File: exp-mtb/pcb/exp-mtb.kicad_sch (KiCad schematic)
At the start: 71 parts, among them J1 Conn_02x08, J2 Conn_02x05, J3 Conn_01x02, J4 Conn_01x02, J5 AVR-ISP-6, Q1 BT148, SW1 SW_Push, U1 ADUM1250, U2 6N137, U3 6N137, U4 ATmega328P-AU, U5 L78L05_SOT89, U6 SN75176AD, U7 PC817, Y1 14.745 MHz

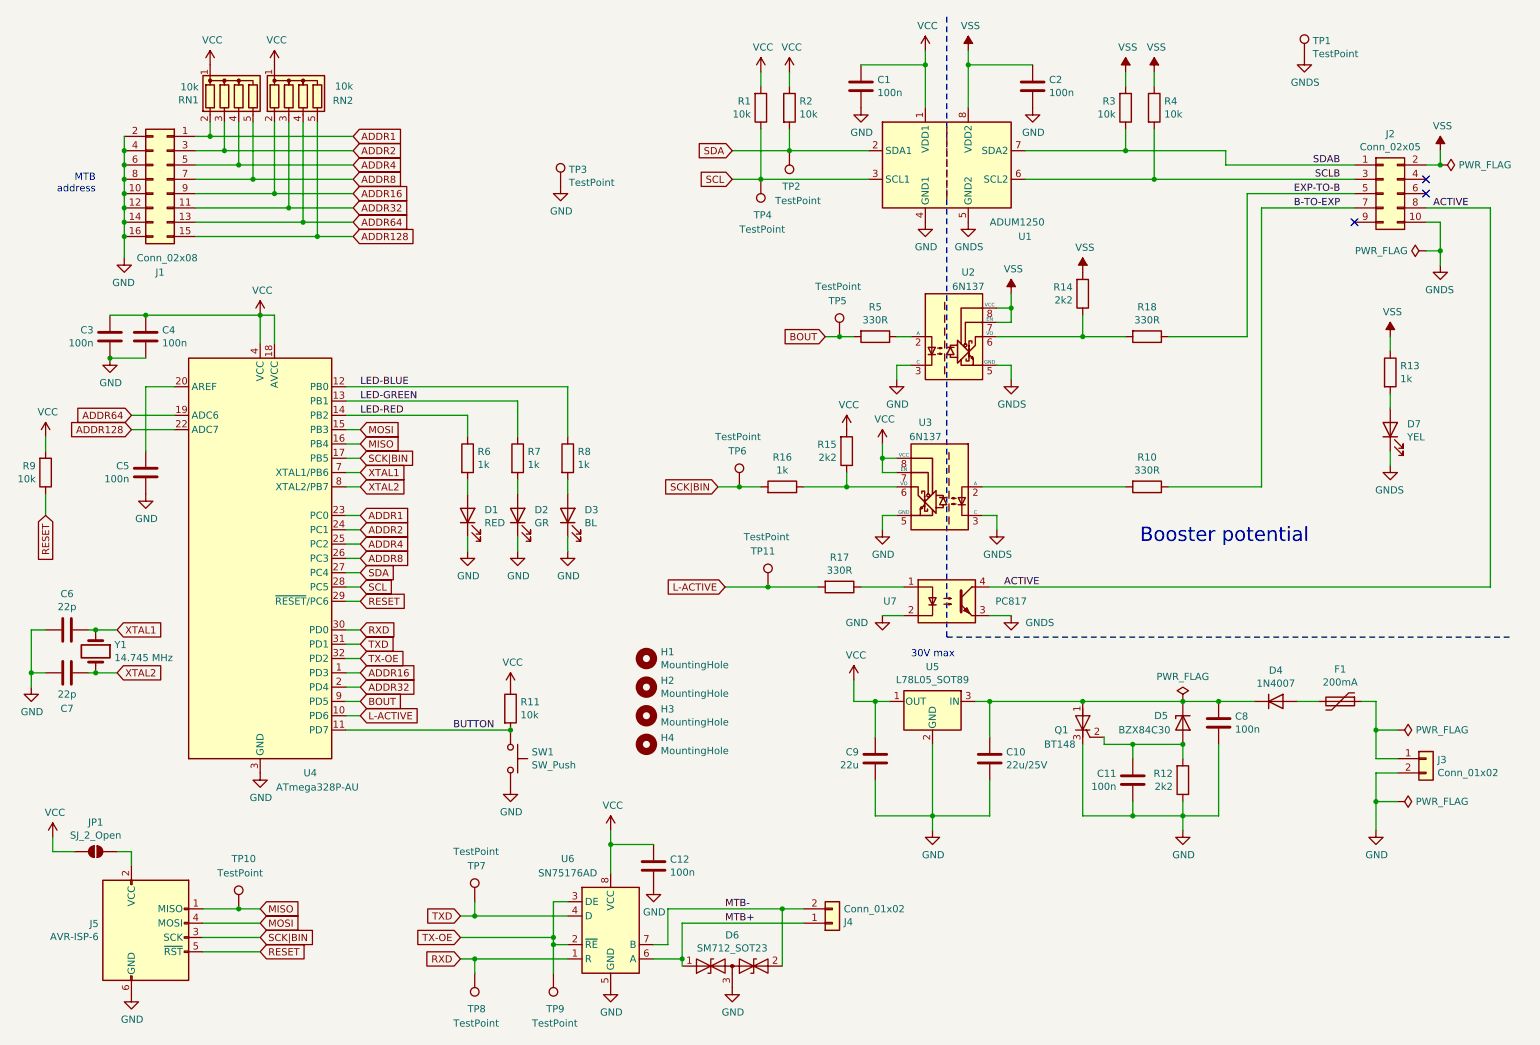
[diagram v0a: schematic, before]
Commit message: exp-mtb: move pcb to 'pcb' directory.
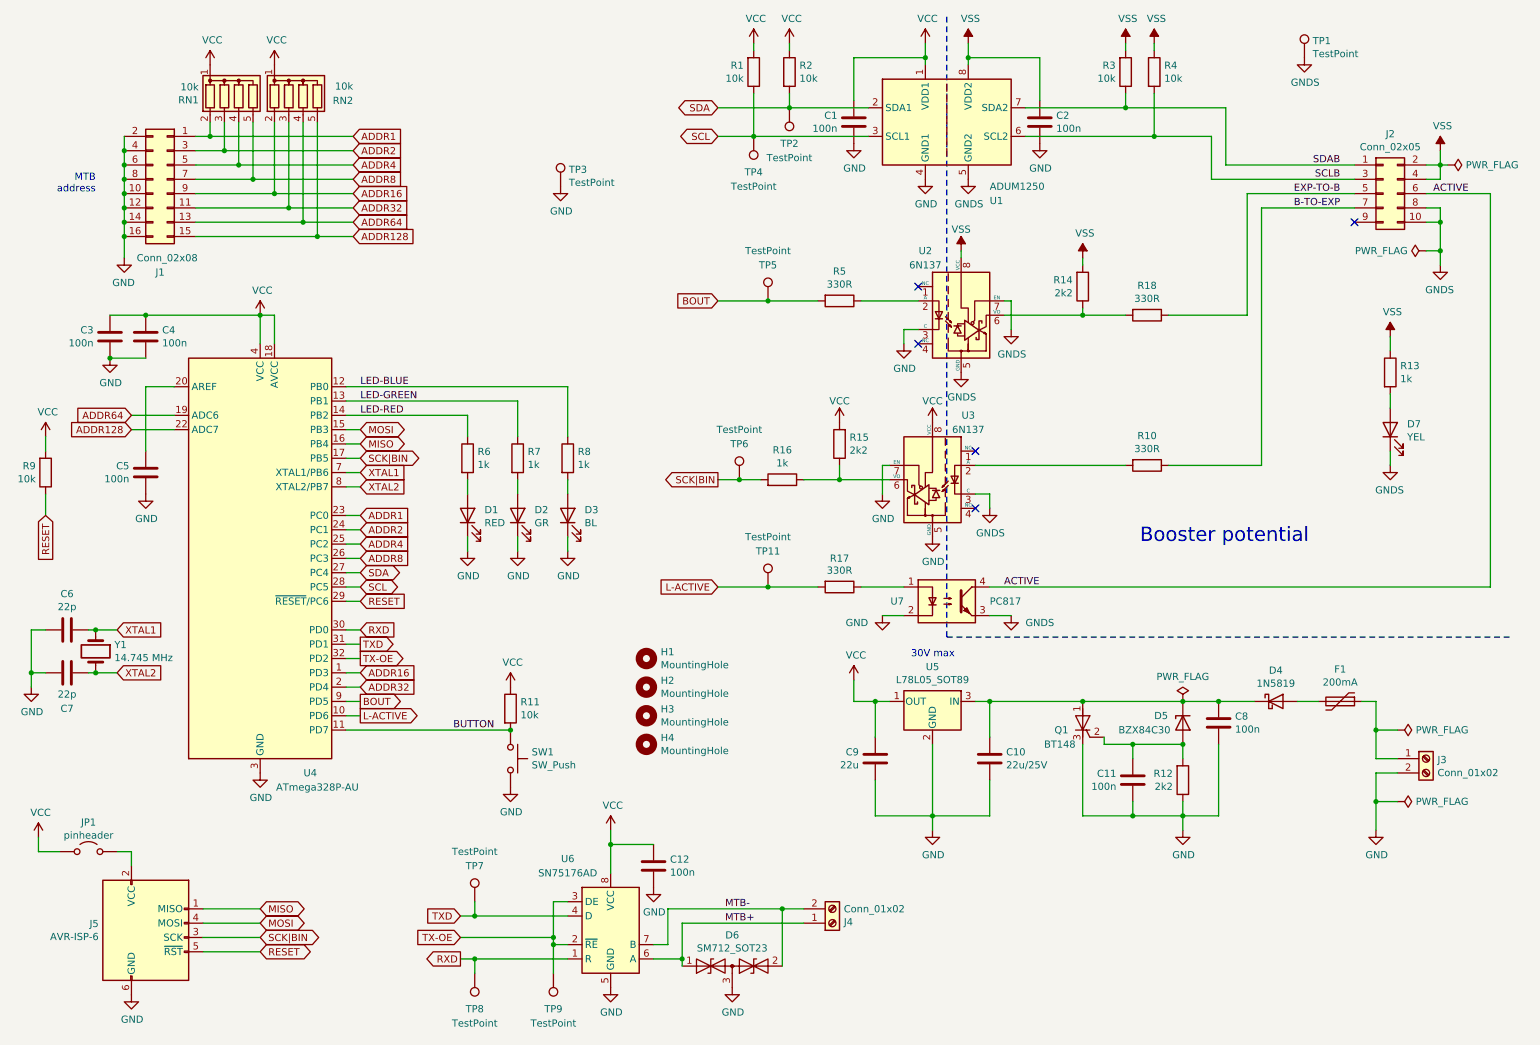
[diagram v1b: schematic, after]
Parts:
- removed TP10: TestPoint, TestPoint:TestPoint_Pad_D1.0mm, symbol Connector:TestPoint
- D4: value 1N4007 -> 1N5819; footprint Diode_SMD:D_SOD-323_HandSoldering -> Diode_SMD:D_SOD-123; symbol Diode:1N4007 -> Diode:1N5819
- D5: footprint Diode_SMD:D_SOT-23_ANK -> Package_TO_SOT_SMD:SOT-23; symbol exp-mtb-rescue:BZX84Cxx-Diode -> Diode:BZX84Cxx
- D6: footprint Package_TO_SOT_SMD:SOT-23_Handsoldering -> Package_TO_SOT_SMD:SOT-23
- J3, J4: symbol Connector_Generic:Conn_01x02 -> Connector:Screw_Terminal_01x02
- JP1: value SJ_2_Open -> pinheader; symbol Jumper:SolderJumper_2_Open -> Jumper:Jumper_2_Open
- Q1: footprint Package_TO_SOT_SMD:SOT-223 -> Package_TO_SOT_THT:TO-92_Inline
- RN1, RN2: footprint Resistor_SMD:R_Array_Concave_4x0603 -> Resistor_THT:R_Array_SIP5
- U2, U3: footprint Package_DIP:SMDIP-8_W7.62mm -> Package_DIP:DIP-8_W7.62mm; symbol exp-mtb-rescue:6N137-Isolator -> Isolator:6N137
- U4: symbol exp-mtb-rescue:ATmega328P-AU-MCU_Microchip_ATmega -> MCU_Microchip_ATmega:ATmega328P-A
- U5: footprint Package_TO_SOT_SMD:SOT-89-3_Handsoldering -> Package_TO_SOT_SMD:SOT-89-3
- U6: footprint Package_DIP:DIP-8_W7.62mm_LongPads -> Package_SO:SOIC-8_3.9x4.9mm_P1.27mm
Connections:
- net ACTIVE: now also J2.6 (Pin_6); no longer J2.8 (Pin_8)
- net GND: now also U3.7 (EN)
- net GNDS: now also J2.8 (Pin_8), U2.7 (EN)
- net VCC: no longer U3.7 (EN)
- net VSS: now also J2.4 (Pin_4); no longer U2.7 (EN)
- net at C10.1, C8.1, D4.1 (K)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: now also D5.3 (K); no longer D5.1 (K)
- net at C11.2, Q1.2 (G), R12.2: now also D5.1 (A); no longer D5.2 (A)
- no-connect marks 3 -> 5
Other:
- moved on the sheet: C1, C2, R1, R10, R14, R15, R16, R18, R2, R3, R4, R5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

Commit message: exp-mtb: remove address jumpers.
Address will be set in EEPROM.
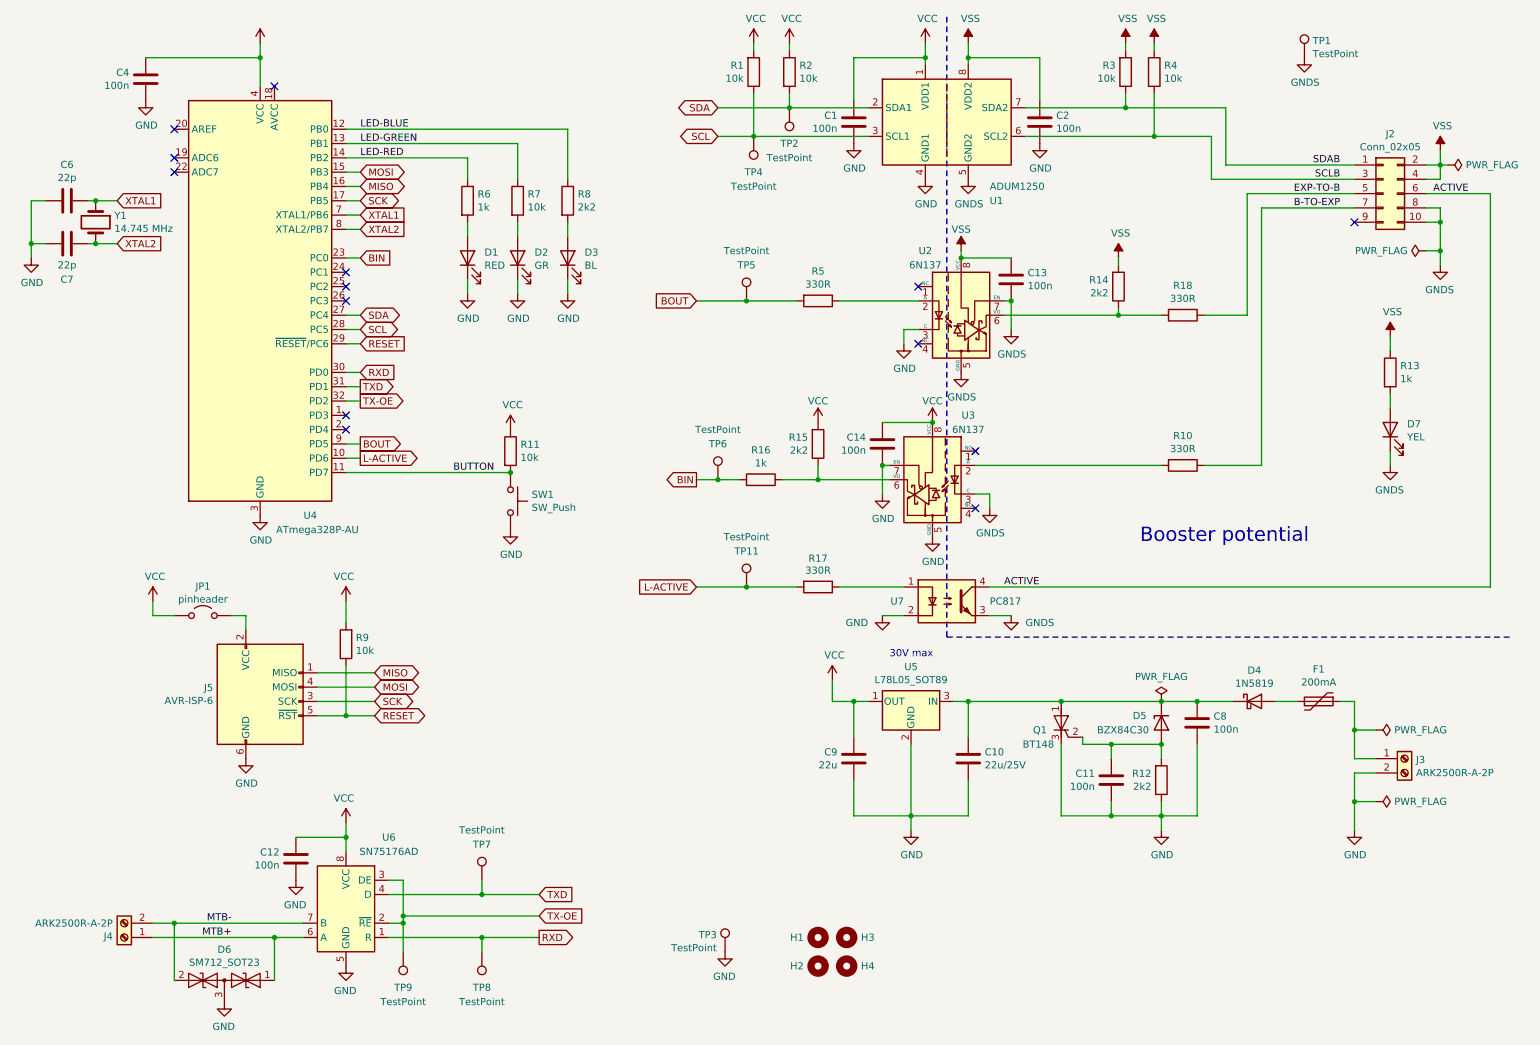
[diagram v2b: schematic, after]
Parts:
- removed C3, C5: 100n, Capacitor_SMD:C_0805_2012Metric_Pad1.18x1.45mm_HandSolder, symbol Device:C
- removed J1: Conn_02x08, Connector_PinHeader_2.54mm:PinHeader_2x08_P2.54mm_Vertical, symbol Connector_Generic:Conn_02x08_Odd_Even
- removed RN1, RN2: 10k, Resistor_THT:R_Array_SIP5, symbol Device:R_Network04
- added C13, C14: 100n, Capacitor_SMD:C_0805_2012Metric_Pad1.18x1.45mm_HandSolder, symbol Device:C
- H1, H2, H3, H4: value MountingHole -> ~
- J3, J4: value Conn_01x02 -> ARK2500R-A-2P; footprint TerminalBlock:TerminalBlock_bornier-2_P5.08mm -> Connector_Phoenix_MSTB:PhoenixContact_MSTBA_2,5_2-G_1x02_P5.00mm_Horizontal
- JP1: footprint Jumper:SolderJumper-2_P1.3mm_Open_RoundedPad1.0x1.5mm -> Connector_PinHeader_2.54mm:PinHeader_1x02_P2.54mm_Vertical
- R7: value 1k -> 10k
- R8: value 1k -> 2k2
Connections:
- net GND: now also C14.2
- net GNDS: now also C13.2
- net VCC: now also C14.1; no longer U4.18 (AVCC)
- net VSS: now also C13.1
- net ADDR1 renamed BIN
- net BIN: now also R16.2, TP6.1
- net ADDR128: no longer names the net of U4.22 (ADC7)
- net ADDR16: no longer names the net of U4.1 (PD3)
- net ADDR2: no longer names the net of U4.24 (PC1)
- net ADDR32: no longer names the net of U4.2 (PD4)
- net ADDR4: no longer names the net of U4.25 (PC2)
- net ADDR64: no longer names the net of U4.19 (ADC6)
- net ADDR8: no longer names the net of U4.26 (PC3)
- net SCK|BIN renamed SCK
- net SCK: no longer R16.2, TP6.1
- no-connect marks 5 -> 14
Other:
- note removed: "MTB address"
- moved on the sheet: C10, C11, C12, C4, C6, C7, C8, C9, D1, D2, D3, D4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

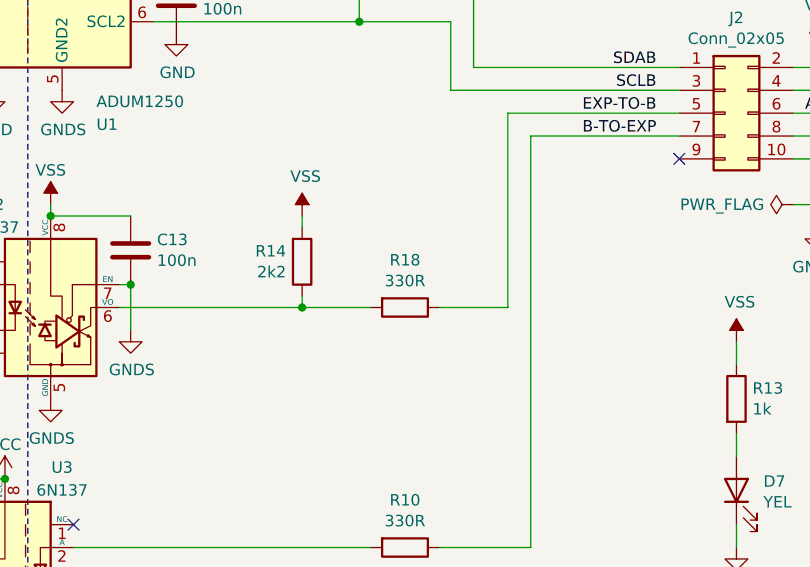
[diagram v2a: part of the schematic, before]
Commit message: Use polyfuse instead of resistor for main-exp protection.
Make voltage measurement possible.
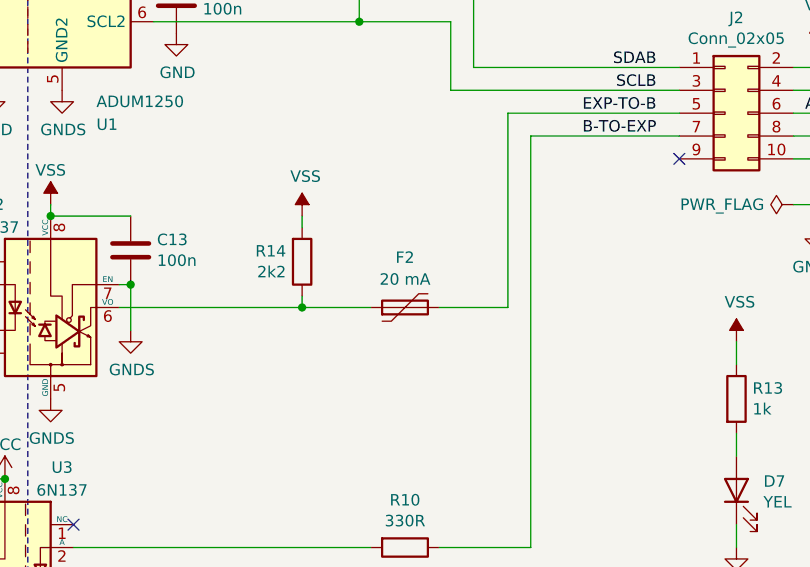
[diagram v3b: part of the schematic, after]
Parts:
- removed R18: 330R, Resistor_SMD:R_0805_2012Metric_Pad1.20x1.40mm_HandSolder, symbol Device:R
- added F2: 20 mA, symbol Device:Polyfuse
- U2, U3: footprint Package_DIP:DIP-8_W7.62mm -> Package_DIP:DIP-8_W8.89mm_SMDSocket_LongPads
- U7: footprint Package_DIP:DIP-4_W7.62mm -> Package_DIP:DIP-4_W8.89mm_SMDSocket_LongPads
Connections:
- net EXP-TO-B: now also F2.2
- net at R14.1, U2.6 (VO): now also F2.1
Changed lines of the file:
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@@
 			)
 		)
-		(property "Footprint" "Package_DIP:DIP-4_W7.62mm"
+		(property "Footprint" "Package_DIP:DIP-4_W8.89mm_SMDSocket_LongPads"
 			(at 175.26 123.19 0)
 			(effects
@@
 	(symbol
 		(lib_id "Device:R")
-		(at 222.25 67.31 270)
-		(unit 1)
-		(exclude_from_sim no)
-		(in_bom yes)
-		(on_board yes)
-		(dnp no)
-		(property "Reference" "R18"
-			(at 222.25 62.0522 90)
-			(effects
-				(font
-					(size 1.27 1.27)
-				)
-			)
-		)
-		(property "Value" "330R"
-			(at 222.25 64.3636 90)
-			(effects
-				(font
-					(size 1.27 1.27)
-				)
-			)
-		)
-		(property "Footprint" "Resistor_SMD:R_0805_2012Metric_Pad1.20x1.40mm_HandSolder"
-			(at 222.25 65.532 90)
-			(effects
-				(font
-					(size 1.27 1.27)
-				)
-				(hide yes)
-			)
-		)
-		(property "Datasheet" "~"
-			(at 222.25 67.31 0)
-			(effects
-				(font
-					(size 1.27 1.27)
-				)
-				(hide yes)
-			)
-		)
-		(property "Description" "Resistor"
-			(at 222.25 67.31 0)
-			(effects
-				(font
-					(size 1.27 1.27)
-				)
-				(hide yes)
-			)
-		)
-		(property "LCSC" "C17513"
-			(at 222.25 67.31 0)
-			(effects
-				(font
-					(size 1.27 1.27)
-				)
-				(hide yes)
-			)
-		)
-		(pin "1"
-		)
-		(pin "2"
-		)
-		(instances
-			(project ""
-				(path "/c8202966-70b9-4a21-a8e6-68d3d7f3ade9"
-					(reference "R18")
-					(unit 1)
-				)
-			)
-		)
-	)
-	(symbol
-		(lib_id "Device:R")
 		(at 210.82 62.23 0)
 		(mirror x)
@@
 			)
 		)
-		(property "Footprint" "Package_DIP:DIP-8_W7.62mm"
+		(property "Footprint" "Package_DIP:DIP-8_W8.89mm_SMDSocket_LongPads"
 			(at 182.88 80.01 0)
 			(effects
@@
 			)
 		)
-		(property "Footprint" "Package_DIP:DIP-8_W7.62mm"
+		(property "Footprint" "Package_DIP:DIP-8_W8.89mm_SMDSocket_LongPads"
 			(at 177.8 109.22 0)
 			(effects
@@
 					(unit 1)
 				)
+			)
+		)
+	)
+	(symbol
+		(lib_id "Device:Polyfuse")
+		(at 222.25 67.31 90)
+		(unit 1)
+		(exclude_from_sim no)
+		(in_bom yes)
+		(on_board yes)
+		(dnp no)
+		(fields_autoplaced yes)
+		(property "Reference" "F2"
+			(at 222.25 61.7685 90)
+			(effects
+				(font
+					(size 1.27 1.27)
+				)
+			)
+		)
+		(property "Value" "20 mA"
+			(at 222.25 64.1928 90)
+			(effects
+				(font
+					(size 1.27 1.27)
+				)
+			)
+		)
+		(property "Footprint" ""
+			(at 227.33 66.04 0)
+			(effects
+				(font
+					(size 1.27 1.27)
+				)
+				(justify left)
+				(hide yes)
+			)
+		)
+		(property "Datasheet" "~"
+			(at 222.25 67.31 0)
+			(effects
+				(font
+					(size 1.27 1.27)
+				)
+				(hide yes)
+			)
+		)
+		(property "Description" "Resettable fuse, polymeric positive temperature coefficient"
+			(at 222.25 67.31 0)
+			(effects
+				(font
+					(size 1.27 1.27)
+				)
+				(hide yes)
+			)
+		)
+		(pin "1"
+		)
+		(pin "2"
+		)
+		(instances
+			(project ""
+				(path "/c8202966-70b9-4a21-a8e6-68d3d7f3ade9"
+					(reference "F2")
+					(unit 1)
+				)
